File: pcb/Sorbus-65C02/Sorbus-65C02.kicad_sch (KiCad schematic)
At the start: 9 parts, among them J1 Conn_01x32_Pin, U1 W65C02SxP

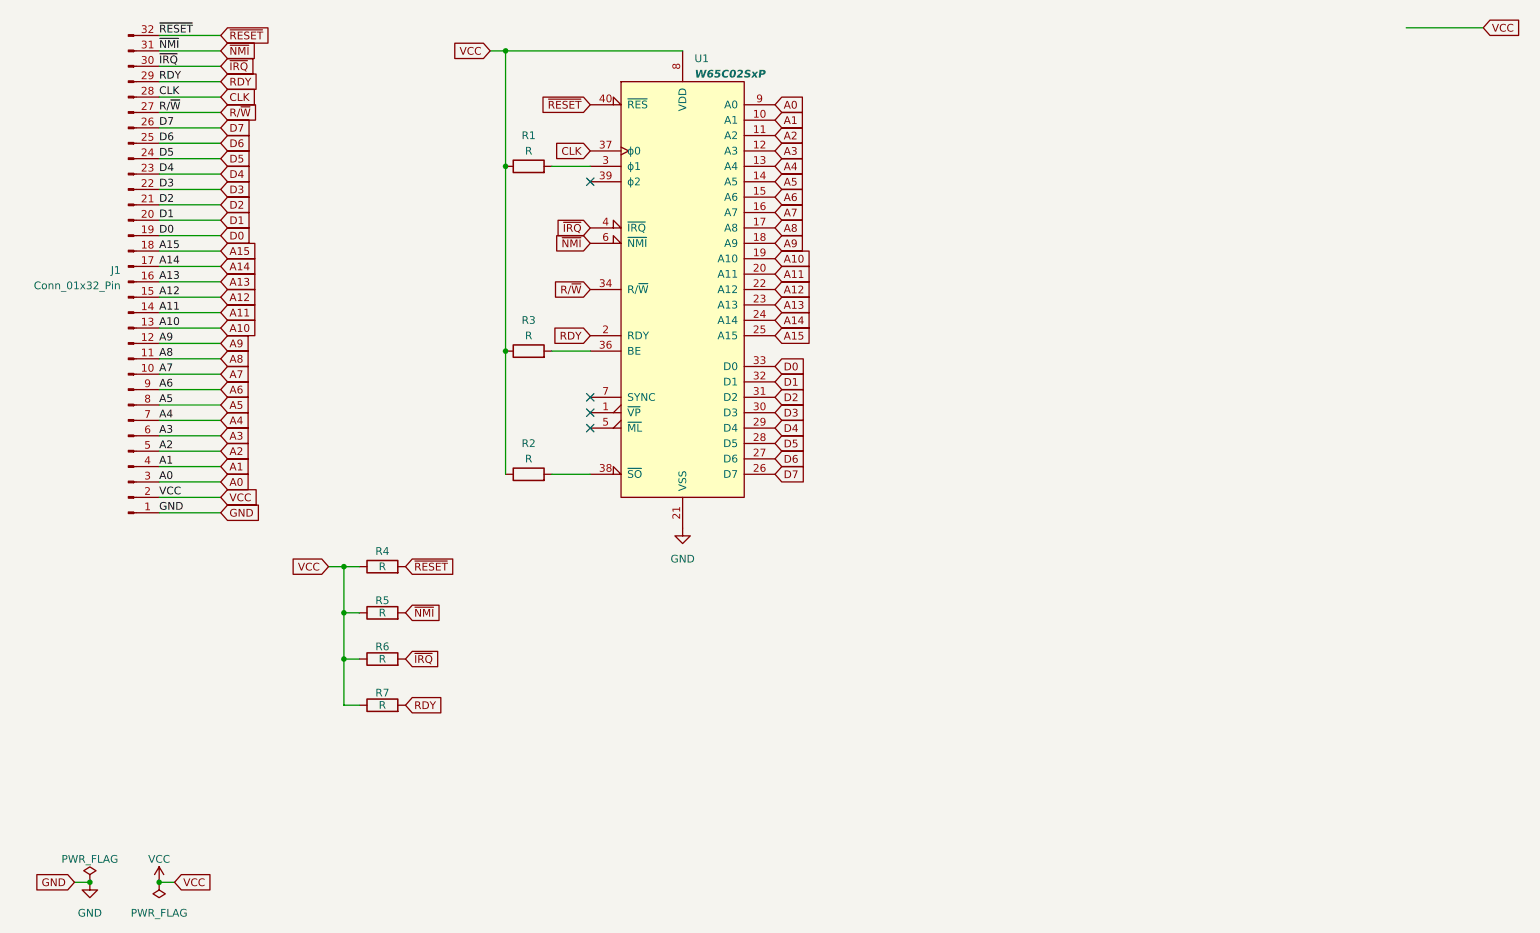
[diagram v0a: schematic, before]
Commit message: updated PCB design - added decoupling capacitor to 65C02 board - replaced simple connectors with real RP2040 Purple component - also updated gerber file and PDF exports from PCB changes - fixed problem in bare build
Signed-off-by: Sven Oliver Moll <svolli@svolli.de>
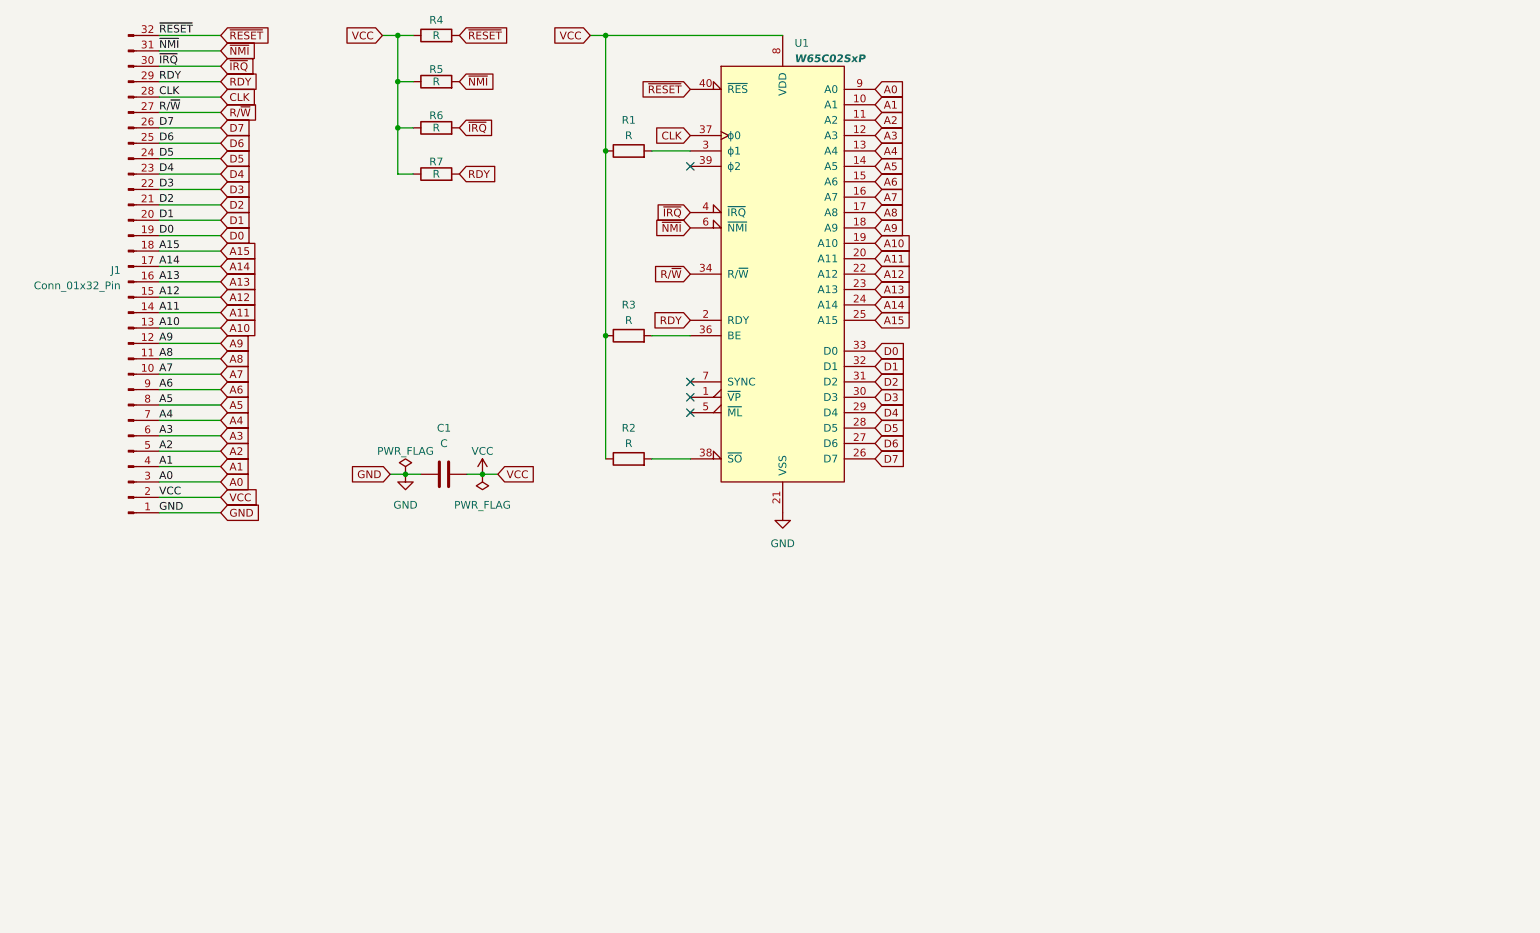
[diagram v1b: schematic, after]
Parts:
- added C1: C, Capacitor_THT:C_Disc_D5.0mm_W2.5mm_P5.00mm, symbol Device:C
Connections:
- net GND: now also C1.1
- net VCC: now also C1.2
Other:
- title: (none) -> Sorbus Computer 65C02
- moved on the sheet: R1, R2, R3, R4, R5, R6, R7, U1
